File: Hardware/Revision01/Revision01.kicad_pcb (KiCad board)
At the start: 4 copper layers, 100 x 119.8 mm, 97 parts, among them J1 Battery connector, J21 StrainConn, J22 StrainConn, J23 StrainConn, J24 StrainConn, J25 StrainConn, J26 StrainConn, J27 StrainConn, J28 StrainConn, J4 Conn_01x03, Q3 NMOS, Q4 PMOS, Q6 PMOS, SW2 SW_SPST_LED, U1 NUCLEO-L476RG, U10 NCP1117LPST50T3G, U2 MRF89XAM9AT-I/RM, U4 ICM-45605

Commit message: random stuff added
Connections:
- net Net-(J21-Pin_2) renamed /Application/StrainOut_AIN8_D-
- net Net-(J21-Pin_3) renamed /Application/StrainOut_AIN8_D+
- net Net-(J22-Pin_2) renamed /Application/StrainOut_AIN7_D-
- net Net-(J22-Pin_3) renamed /Application/StrainOut_AIN7_D+
- net Net-(J23-Pin_2) renamed /Application/StrainOut_AIN6_D-
- net Net-(J23-Pin_3) renamed /Application/StrainOut_AIN6_D+
- net Net-(J24-Pin_2) renamed /Application/StrainOut_AIN5_D-
- net Net-(J24-Pin_3) renamed /Application/StrainOut_AIN5_D+
- net Net-(J25-Pin_2) renamed /Application/StrainOut_AIN4_D-
- net Net-(J25-Pin_3) renamed /Application/StrainOut_AIN4_D+
- net Net-(J26-Pin_2) renamed /Application/StrainOut_AIN3_D-
- net Net-(J26-Pin_3) renamed /Application/StrainOut_AIN3_D+
- net Net-(J27-Pin_2) renamed /Application/StrainOut_AIN2_D-
- net Net-(J27-Pin_3) renamed /Application/StrainOut_AIN2_D+
- net Net-(J28-Pin_2) renamed /Application/StrainOut_AIN1_D-
- net Net-(J28-Pin_3) renamed /Application/StrainOut_AIN1_D+
- R21 pad 1: /Application/AIN1_D- -> /Application/AIN1_D+
- R22 pad 1: /Application/AIN1_D+ -> /Application/AIN1_D-
- R23 pad 1: unconnected-(R23-Pad1) -> /Application/AIN2_D+
- R24 pad 1: unconnected-(R24-Pad1) -> /Application/AIN2_D-
- R25 pad 1: unconnected-(R25-Pad1) -> /Application/AIN3_D+
- R26 pad 1: unconnected-(R26-Pad1) -> /Application/AIN3_D-
- R27 pad 1: unconnected-(R27-Pad1) -> /Application/AIN4_D+
- R28 pad 1: unconnected-(R28-Pad1) -> /Application/AIN4_D-
- R29 pad 1: unconnected-(R29-Pad1) -> /Application/AIN5_D+
- R30 pad 1: unconnected-(R30-Pad1) -> /Application/AIN5_D-
- R31 pad 1: unconnected-(R31-Pad1) -> /Application/AIN6_D+
- R32 pad 1: unconnected-(R32-Pad1) -> /Application/AIN6_D-
- R33 pad 1: unconnected-(R33-Pad1) -> /Application/AIN7_D+
- R34 pad 1: unconnected-(R34-Pad1) -> /Application/AIN7_D-
- R35 pad 1: unconnected-(R35-Pad1) -> /Application/AIN8_D+
- R36 pad 1: unconnected-(R36-Pad1) -> /Application/AIN8_D-
- U1 pad CN10_11: /BatteryV_Measurement_ADC12_IN10 -> /BatteryV_Measurement_ADC12_IN1
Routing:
- net /Application/StrainOut_AIN8_D+: track 0.00 -> 63.6 mm, vias 0 -> 1
- net /Application/StrainOut_AIN3_D+: track 0.00 -> 60.9 mm
- net /Application/StrainOut_AIN8_D-: track 0.00 -> 60.7 mm, vias 0 -> 1
- net /Application/StrainOut_AIN3_D-: track 0.00 -> 60.2 mm
- net /Application/StrainOut_AIN2_D-: track 0.00 -> 57.0 mm
- net /Application/StrainOut_AIN2_D+: track 0.00 -> 52.8 mm
- net /Application/StrainOut_AIN1_D+: track 0.00 -> 51.1 mm
- net /Application/StrainOut_AIN1_D-: track 0.00 -> 49.6 mm
- net /Application/+StrainV: track 333.9 -> 306.2 mm
- net (no net): track 9.30 -> 0.42 mm

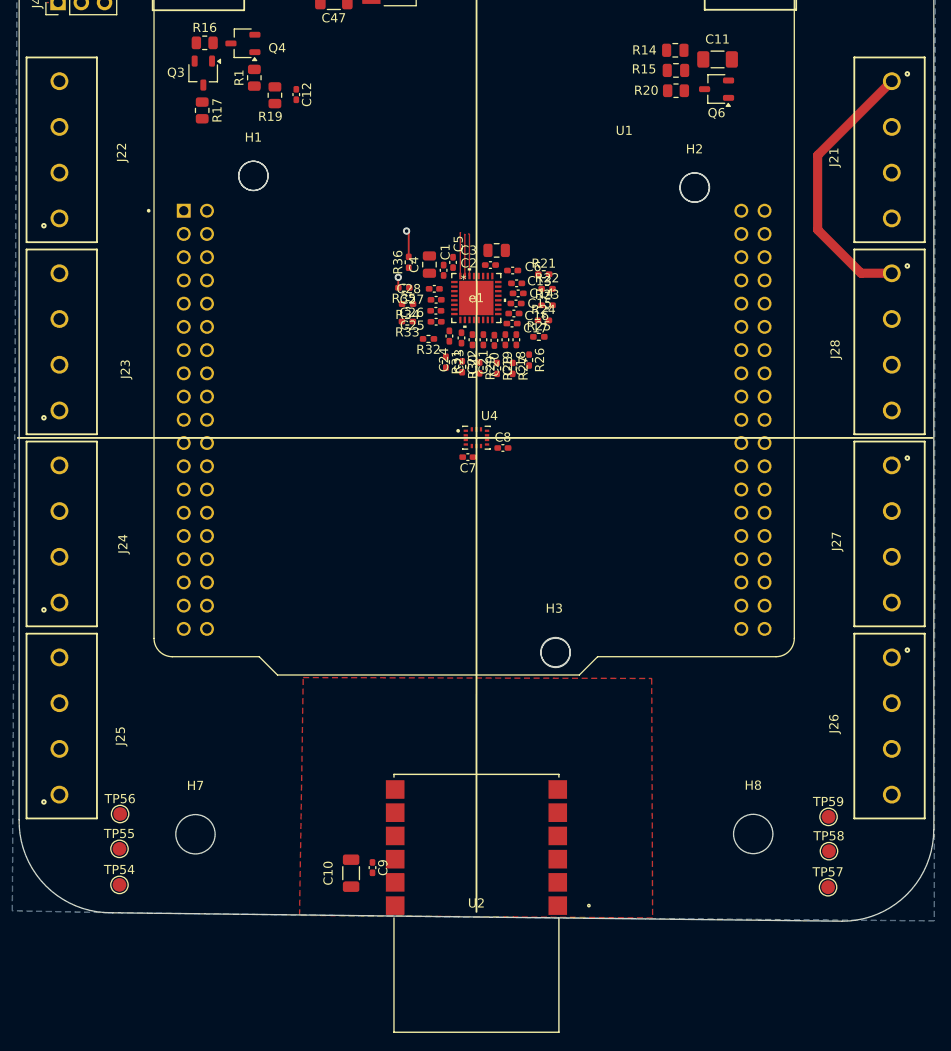
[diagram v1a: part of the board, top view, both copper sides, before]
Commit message: some feedback implemented, MISO/MOSI SIWTCHED, GPIO_USB_5V FIXED, COMMENTS REGARDING ALTERNATIVE ADC's, and PCB CONNECTED TO EXTERNAL GND added
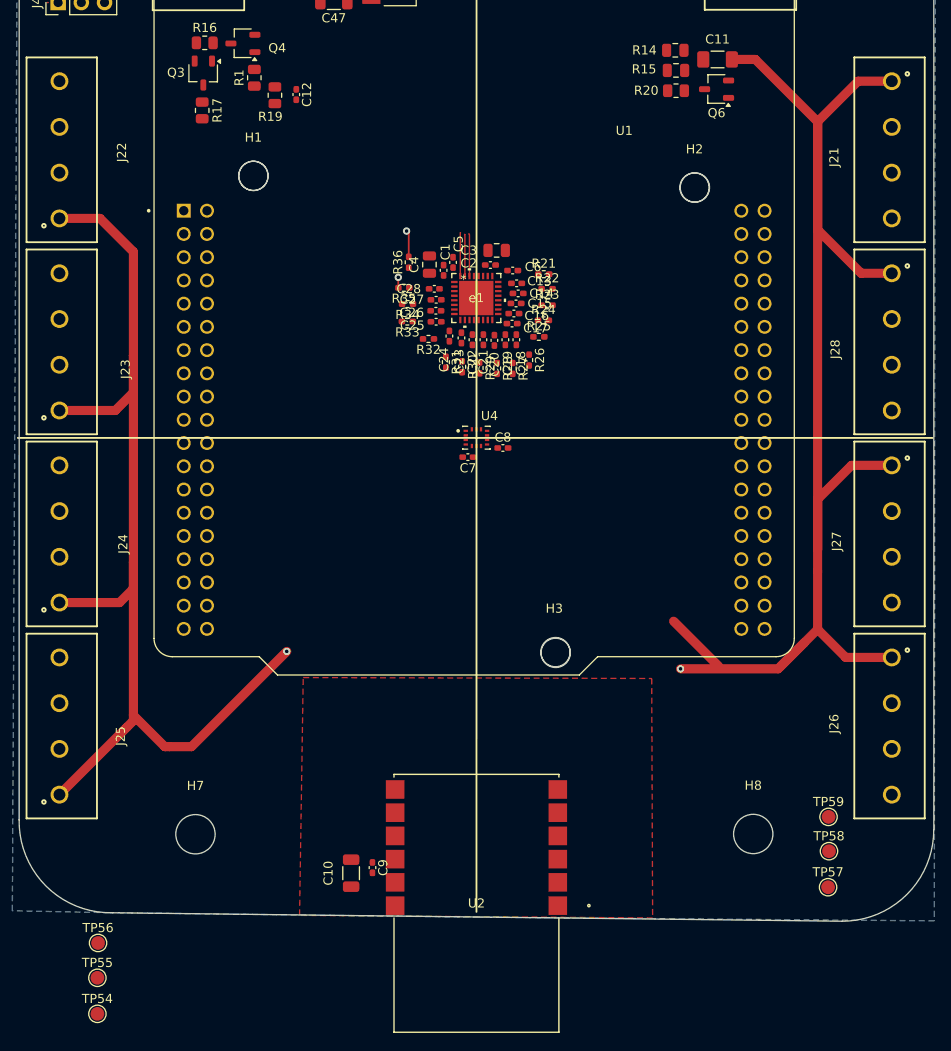
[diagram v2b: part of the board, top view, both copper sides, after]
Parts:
- moved TP54 14.3 mm to (119.6, 162.8)
- moved TP55 14.3 mm to (119.6, 158.9)
- moved TP56 14.3 mm to (119.7, 155.1)
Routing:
- net /Application/StrainOut_AIN5_D+: track 0.00 -> 52.1 mm
- net /Application/StrainOut_AIN5_D-: track 0.00 -> 51.0 mm
- net /Application/StrainOut_AIN4_D-: track 0.00 -> 44.7 mm
- net /Application/StrainOut_AIN4_D+: track 0.00 -> 44.3 mm
- net /Application/StrainOut_AIN7_D+: track 0.00 -> 35.4 mm
- net /Application/StrainOut_AIN7_D-: track 0.00 -> 35.0 mm
- net /Application/+StrainV: track 306.2 -> 319.9 mm, vias 0 -> 2

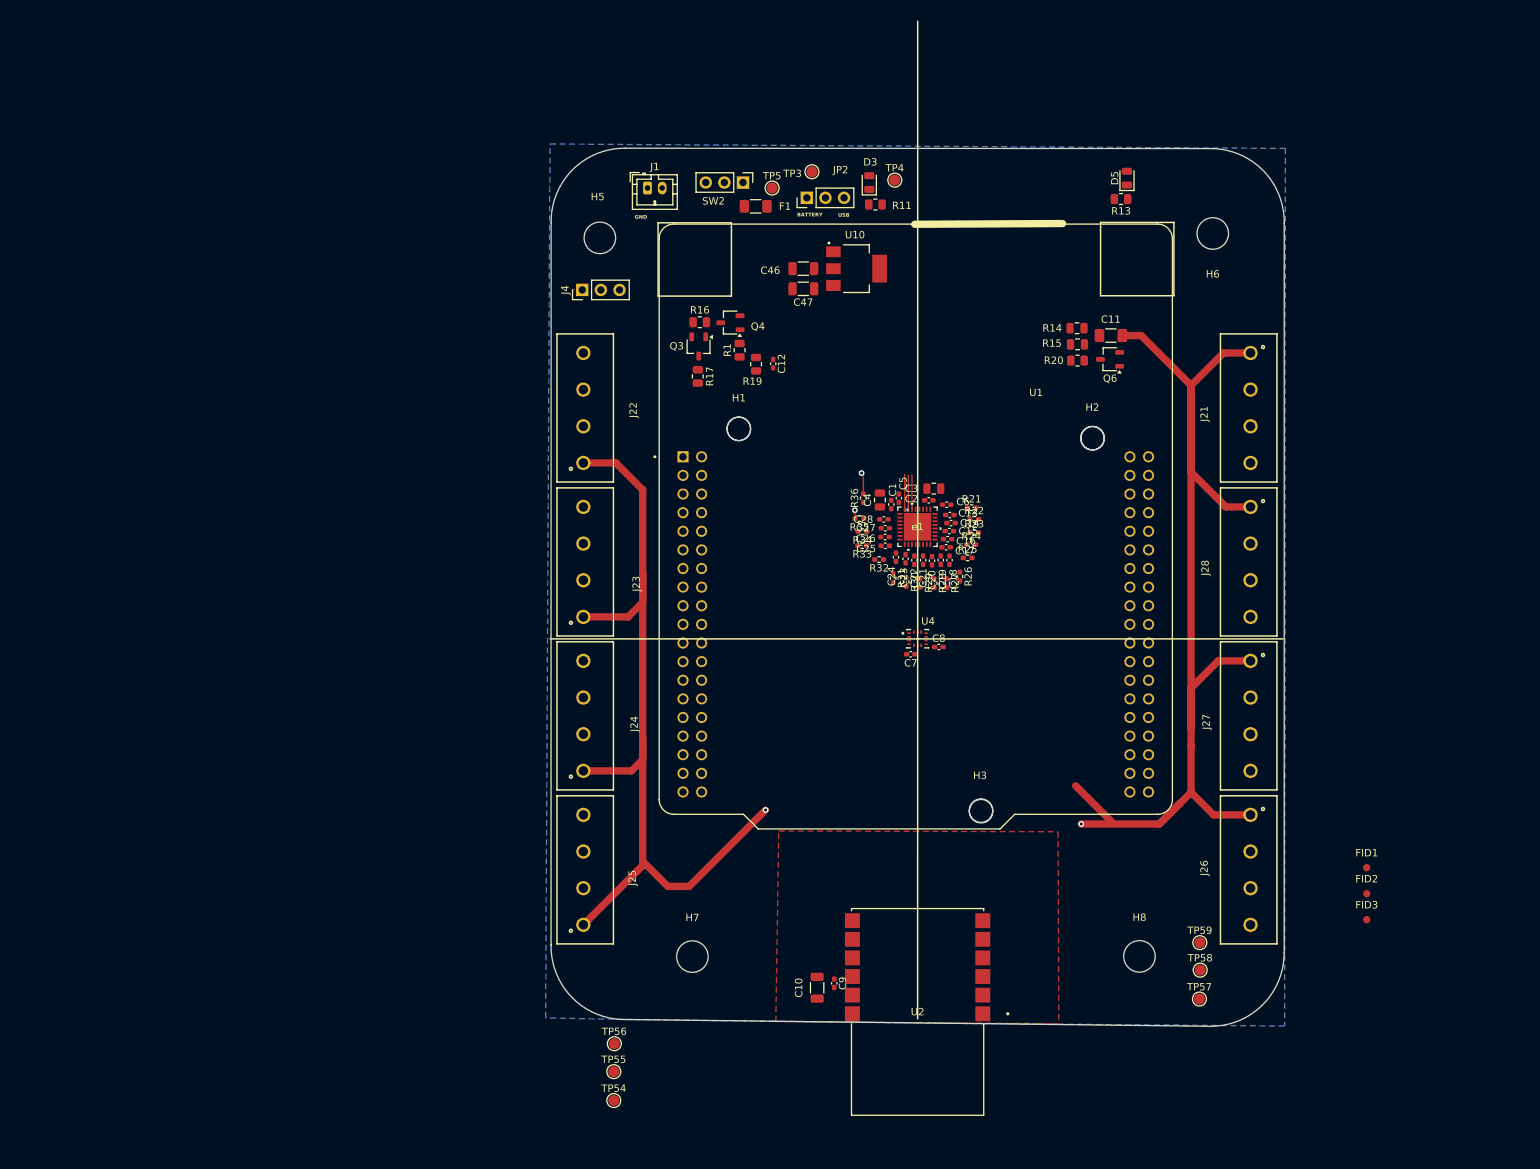
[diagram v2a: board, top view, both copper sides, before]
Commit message: Implemented new more reliable design utilizing instrumentation amplifiers
Changed RESISTORS for new Power requirements
Added prototype features of breathing cube to test out.
Removed MCU sheet, as moving pins around was getting too messy
Picked out Instrumentation OP-AMP, INA331 or INA2331
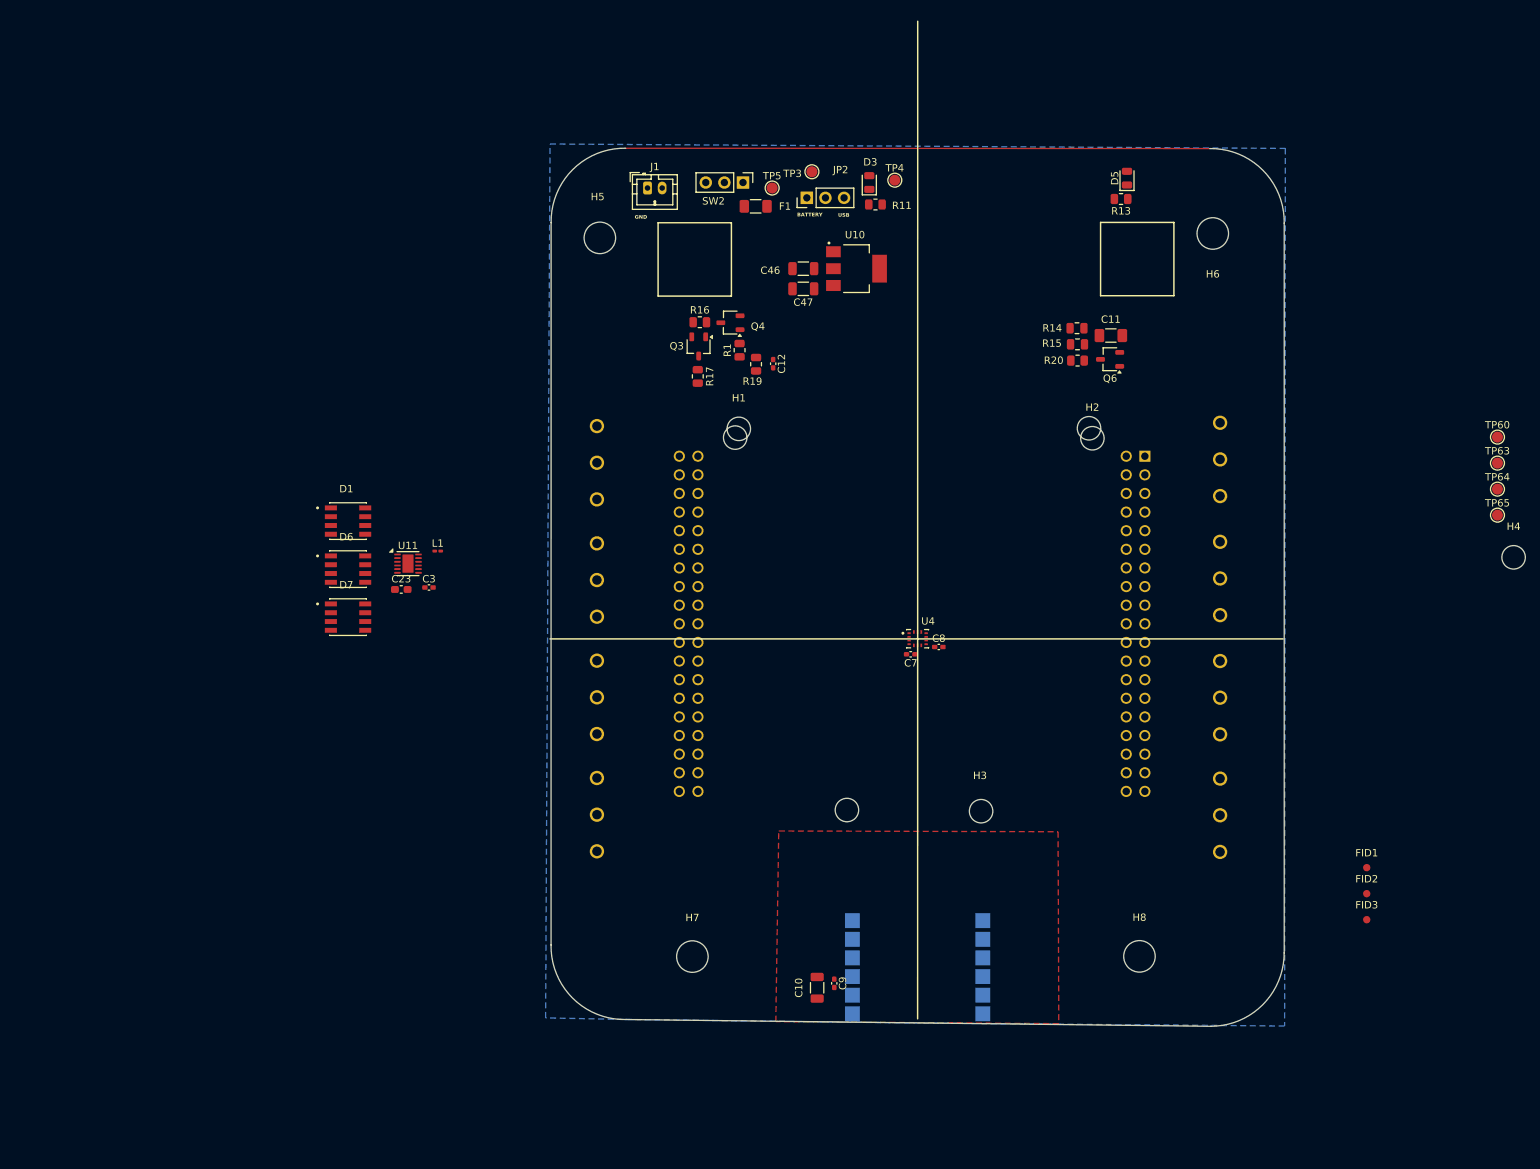
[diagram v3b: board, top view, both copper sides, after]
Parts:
- removed C1, C13, C14, C15, C16, C17, C18, C19, C2, C20, C21, C22, C24, C25, C26, C27, C28, C5, C6: 0.1uF, Capacitor_SMD:C_0402_1005Metric_Pad0.74x0.62mm_HandSolder
- removed C4: 1uF, Capacitor_SMD:C_0805_2012Metric
- removed J21, J22, J23, J24, J25, J26, J27, J28: StrainConn, 691137710004:691137710004
- removed R21, R22, R23, R24, R25, R26, R27, R28, R29, R30, R31, R32, R33, R34, R35, R36: 1K, Resistor_SMD:R_0402_1005Metric_Pad0.72x0.64mm_HandSolder
- removed TP54, TP55, TP56, TP57, TP58, TP59: TestPoint, TestPoint:TestPoint_Pad_D1.5mm
- removed U1: NUCLEO-L476RG, NUCLEO-L476RG:MODULE_NUCLEO-L476RG
- removed e1: AD7124-8BCPZ-RL7-adc, AD7124-8BCPZ-RL7-adc:CP-32-12_ADI-L
- added D1: RGBW_LED, RGBW:SOL120P540X160-8N, F.Cu at (83.3, 83.8)
- added D6: RGBW_LED, RGBW:SOL120P540X160-8N, F.Cu at (83.3, 90.4)
- added D7: RGBW_LED, RGBW:SOL120P540X160-8N, F.Cu at (83.3, 96.9)
- added H4: MountingHole, MountingHole:MountingHole_3.2mm_M3, F.Cu at (242.3, 88.8)
- added J2: StrainConn, 691137710003:691137710003, B.Cu at (117.3, 123.9)
- added J3: StrainConn, 691137710003:691137710003, B.Cu at (117.3, 107.9)
- added J5: StrainConn, 691137710003:691137710003, B.Cu at (117.3, 75.9)
- added J6: StrainConn, 691137710003:691137710003, B.Cu at (202.3, 123.9)
- added J7: StrainConn, 691137710003:691137710003, B.Cu at (202.3, 91.6)
- added J8: StrainConn, 691137710003:691137710003, B.Cu at (202.3, 75.4)
- added J9: StrainConn, 691137710003:691137710003, B.Cu at (202.3, 107.9)
- added L1: 1uH, Inductor_SMD:L_0201_0603Metric_Pad0.64x0.40mm_HandSolder, F.Cu at (95.6, 87.9)
- added TP60: TestPoint, TestPoint:TestPoint_Pad_D1.5mm, F.Cu at (240.1, 72.4)
- added TP63: TestPoint, TestPoint:TestPoint_Pad_D1.5mm, F.Cu at (240.1, 75.9)
- added TP64: TestPoint, TestPoint:TestPoint_Pad_D1.5mm, F.Cu at (240.1, 79.5)
- added TP65: TestPoint, TestPoint:TestPoint_Pad_D1.5mm, F.Cu at (240.1, 83.0)
- added U11: LP5813BDRRR, Package_SON:WSON-12-1EP_3x3mm_P0.5mm_EP1.5x2.5mm, F.Cu at (91.5, 89.6)
- added U3: NUCLEO-L476RG, NUCLEO-L476RG:MODULE_NUCLEO-L476RG, B.Cu at (160.3, 84.5)
- C23: value 0.1uF -> 22uF; footprint Capacitor_SMD:C_0402_1005Metric_Pad0.74x0.62mm_HandSolder -> Capacitor_SMD:C_0603_1608Metric_Pad1.08x0.95mm_HandSolder
- C3: value 1uF -> 10uF; footprint Capacitor_SMD:C_0805_2012Metric -> Capacitor_SMD:C_0402_1005Metric_Pad0.74x0.62mm_HandSolder
- J4: value Conn_01x03 -> StrainConn; footprint Connector_PinHeader_2.54mm:PinHeader_1x03_P2.54mm_Vertical -> 691137710003:691137710003; moved to B.Cu
- U2: moved to B.Cu
- moved C3 70.2 mm to (94.4, 92.9)
- moved C23 68.9 mm to (90.6, 93.1), turned to 0 degrees
- moved J4 39.6 mm to (117.3, 91.9), turned to -90 degrees
- turned U2 to 0 degrees
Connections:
- net /BatteryV_Measurement_ADC12_IN10 renamed /BatteryV_AIN
- net /PC5_GPIO renamed Net-(D3-K)
- C23 pad 1: /Application/AIN6_D+ -> Net-(U11-VOUT)
- J4 pad 1: Net-(J4-Pin_1) -> /Application/+StrainV
- J4 pad 2: Net-(J4-Pin_2) -> /AIN_3
- J4 pad 3: Net-(J4-Pin_3) -> GND
- R14 pad 2: +3.3V -> +5V
- R15 pad 2: +5V -> +3.3V
- U2 pad 5: /PB14_SPI2_MISO -> /PB15_SPI2_MOSI
- U2 pad 7: /PB15_SPI2_MOSI -> /PB14_SPI2_MISO
- U2 pad 8: /ANT_CS_ActiveLow_GPIO -> /ANT_CSDATA_GPIO
- U4 pad 1: /PB15_SPI2_MOSI -> /PB14_SPI2_MISO
- U4 pad 14: /PB14_SPI2_MISO -> /PB15_SPI2_MOSI
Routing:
- net /Application/+StrainV: track 319.9 -> 0.00 mm, vias 2 -> 0
- net /Application/StrainOut_AIN8_D+: track 63.6 -> 0.00 mm, vias 1 -> 0
- net /Application/StrainOut_AIN3_D+: track 60.9 -> 0.00 mm
- net /Application/StrainOut_AIN8_D-: track 60.7 -> 0.00 mm, vias 1 -> 0
- net /Application/StrainOut_AIN3_D-: track 60.2 -> 0.00 mm
- net /Application/StrainOut_AIN2_D-: track 57.0 -> 0.00 mm
- net /Application/StrainOut_AIN2_D+: track 52.8 -> 0.00 mm
- net /Application/StrainOut_AIN5_D+: track 52.1 -> 0.00 mm
- net /Application/StrainOut_AIN1_D+: track 51.1 -> 0.00 mm
- net /Application/StrainOut_AIN5_D-: track 51.0 -> 0.00 mm
- net /Application/StrainOut_AIN1_D-: track 49.6 -> 0.00 mm
- net /Application/StrainOut_AIN4_D-: track 44.7 -> 0.00 mm
- net /Application/StrainOut_AIN4_D+: track 44.3 -> 0.00 mm
- net /Application/StrainOut_AIN7_D+: track 35.4 -> 0.00 mm
- net /Application/StrainOut_AIN7_D-: track 35.0 -> 0.00 mm
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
